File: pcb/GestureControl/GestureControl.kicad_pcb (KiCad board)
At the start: 4 copper layers, 95.3 x 87.6 mm, 102 parts, among them J1 Conn_01x04_I2I-LCD, J10 EXTERN I2C, J11 Conn_01x01, J12 Conn_01x01, J13 Conn_01x01, J14 Conn_01x01, J15 Conn_01x01, J16 Conn_01x01, J17 Conn_01x01, J18 Conn_01x01, J19 Conn_01x01, J2 BATT, J3 Conn_01x08, J4 Conn_01x06, J5 Conn_01x10, J6 Conn_01x08, J7 FTDI, J8 Serial Wire, J9 UART, SW1 SW1, SW2 SW2, SW3 BOOT, SW4 RST, U1 LD1117-3.3, U2 LD1117-5.0, U3 VL53L3CXV0DH_CENTER, U4 VL53L3CXV0DH_RIGHT, U5 VL53L3CXV0DH_LEFT, U6 STM32L151RETx, U7 STM32F401RETx, Y1 8MHz, Y2 32kHz

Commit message: eind tekenen PCB
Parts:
- C23, C28, C29, C30, C31, D7, R10, R11: moved to B.Cu
- J10: footprint Connector_PinHeader_2.54mm:PinHeader_1x04_P2.54mm_Horizontal -> Connector_PinHeader_2.54mm:PinHeader_1x04_P2.54mm_Vertical
- J7: footprint Connector_PinHeader_2.54mm:PinHeader_1x06_P2.54mm_Horizontal -> Connector_PinHeader_2.54mm:PinHeader_1x06_P2.54mm_Vertical
- J8: footprint Connector_PinHeader_2.54mm:PinHeader_1x05_P2.54mm_Horizontal -> Connector_PinHeader_2.54mm:PinHeader_1x05_P2.54mm_Vertical
- R1, R2, R3, R4, R5, R6, R7: moved to F.Cu
- moved J7 64.7 mm to (157.0, 63.8), turned to 180 degrees
- moved J8 46.2 mm to (153.2, 61.2), turned to 180 degrees
- moved D7 44.0 mm to (128.8, 101.1), turned to 180 degrees
- moved J19 37.2 mm to (164.3, 47.8), turned to 180 degrees
- moved C4 36.0 mm to (129.0, 89.9), turned to 0 degrees
- moved C3 35.2 mm to (139.4, 89.9), turned to 0 degrees
- moved J18 34.2 mm to (164.3, 50.3), turned to 180 degrees
- moved SW2 33.6 mm to (162.8, 78.2), turned to 180 degrees
- moved D5 31.5 mm to (156.7, 95.2), turned to 90 degrees
- moved C6 31.2 mm to (129.0, 97.3), turned to 0 degrees
- moved R5 30.5 mm to (156.7, 91.2), turned to 90 degrees
- moved R9 30.1 mm to (159.8, 75.9)
- moved C2 30.0 mm to (159.6, 78.0), turned to 180 degrees
- moved J17 29.9 mm to (164.3, 57.9)
- moved J16 28.9 mm to (164.3, 60.5), turned to 180 degrees
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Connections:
- U6 pad 27: (no net) -> SW_1
- U6 pad 28: (no net) -> SW_2
- U7 pad 27: (no net) -> SW_1
- U7 pad 28: (no net) -> SW_2
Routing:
- net GND: track 89.6 -> 206.3 mm, vias 45 -> 29
- net +3V3: track 399.3 -> 506.0 mm, vias 37 -> 21
- net /STM32L151RET6TR/SWDAT: track 80.6 -> 20.3 mm, vias 3 -> 1
- net LED_5: track 94.8 -> 37.5 mm, vias 3 -> 1
- net LED_4: track 95.3 -> 39.3 mm, vias 3 -> 1
- net /STM32L151RET6TR/SW0: track 62.4 -> 23.6 mm, vias 1 -> 2
- net /STM32L151RET6TR/FTDI_TXD: track 53.1 -> 15.6 mm, vias 3 -> 0
- net /STM32L151RET6TR/SWCLK: track 57.5 -> 22.9 mm, vias 1 -> 0
- net /STM32L151RET6TR/FTDI_CTS: track 55.5 -> 22.0 mm, vias 0 -> 1
- net /STM32L151RET6TR/FTDI_RXD: track 50.3 -> 16.9 mm, vias 3 -> 0
- net LED_3: track 73.1 -> 40.9 mm, vias 3 -> 1
- net VCC: track 26.7 -> 55.5 mm, vias 4 -> 6
- net /STM32L151RET6TR/OS32_IN: track 37.0 -> 9.26 mm
- net /STM32L151RET6TR/OS32_OUT: track 35.4 -> 9.99 mm
- net GPIOI_2: track 113.2 -> 90.9 mm
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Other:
- net class PWR added: clearance 0.4, trace_width 0.25, via_dia 0.8, via_drill 0.4
- board text removed: "- +"
- board text removed: "BOOT"
- board text removed: "FTDI"
- board text removed: "I2C LCD"
- board text removed: "RST"
- board text removed: "Serial Wire"
- board text removed: "UART"

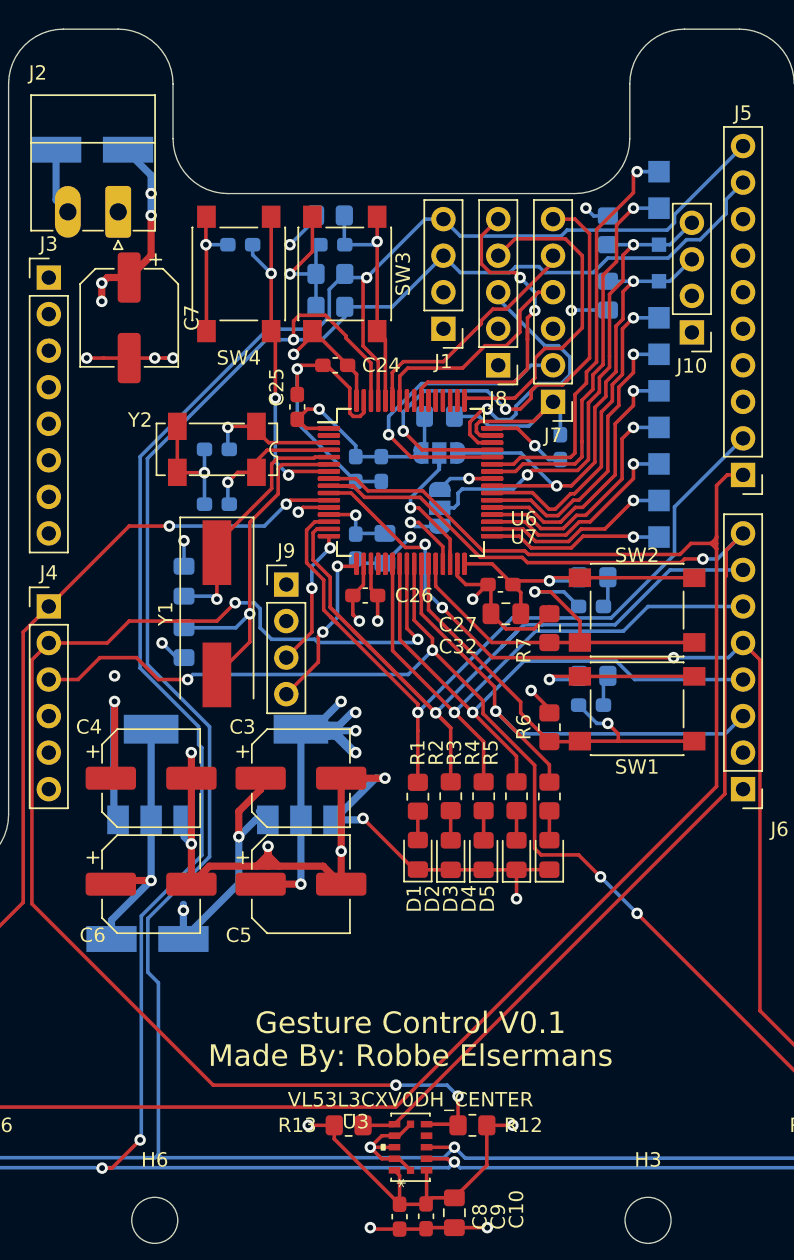
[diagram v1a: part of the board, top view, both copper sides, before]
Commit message: add text pcb
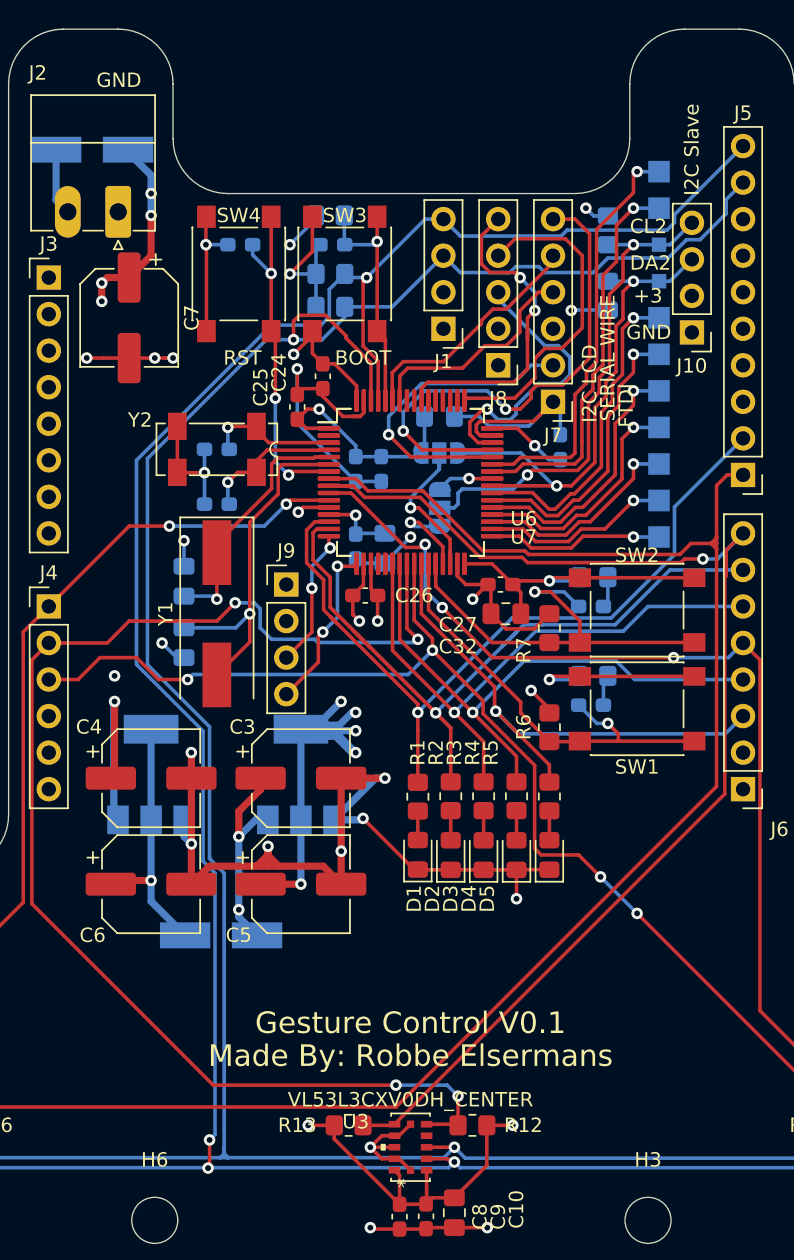
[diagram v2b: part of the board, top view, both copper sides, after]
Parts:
- moved D7 5.13 mm to (133.9, 100.8)
- moved C24 1.15 mm to (141.0, 62.0), turned to 270 degrees
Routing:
- net SCL1: track 195.7 -> 193.2 mm
- net GND: track 206.3 -> 205.5 mm
- net +3V3: track 506.0 -> 506.8 mm
- net +5V: track 109.6 -> 108.8 mm
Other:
- board text added: "+3"
- board text added: "+3.3"
- board text added: "+5"
- board text added: "-"
- board text added: "BOOT"
- board text added: "CL1"
- board text added: "CL2"
- board text added: "CLK"
- board text added: "CTS"
- board text added: "D1"
- board text added: "D2"
- board text added: "D3"
- board text added: "D4"
- board text added: "D5"
- board text added: "DA1"
- board text added: "DA2"
- board text added: "DAT"
- board text added: "F401RETx (U7): JP3 -> 1-2, JP2 -> 2-3"
- board text added: "FTDI"
- board text added: "GND"
- board text added: "GP0"
- board text added: "GP1"
- board text added: "GP2"
- board text added: "I2C LCD"
- board text added: "I2C Slave"
- board text added: "L151RETx (U6): JP3 -> 2-3, JP2 -> 1-2"
- board text added: "PA10 PA9 SCL2 SDA2 PC8 PC7 PC6 PB15 PB14 PB13 PB12"
- board text added: "RST"
- board text added: "RTS"
- board text added: "RX"
- board text added: "SERIAL WIRE"
- board text added: "SW0"
- board text added: "TX"
- board text added: "XS0"
- board text added: "XS1"
- board text added: "XS2"

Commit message: add feedback Philip
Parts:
- added C34: 4.7µ, Capacitor_SMD:C_0805_2012Metric_Pad1.18x1.45mm_HandSolder, F.Cu at (142.0, 102.9)
- added C35: 100n, Capacitor_SMD:C_0603_1608Metric_Pad1.08x0.95mm_HandSolder, B.Cu at (146.8, 111.4)
- added C36: 100n, Capacitor_SMD:C_0603_1608Metric_Pad1.08x0.95mm_HandSolder, B.Cu at (146.8, 128.4)
- added C37: 4.7µ, Capacitor_SMD:C_0805_2012Metric_Pad1.18x1.45mm_HandSolder, B.Cu at (148.8, 111.2)
- added C38: 4.7µ, Capacitor_SMD:C_0805_2012Metric_Pad1.18x1.45mm_HandSolder, B.Cu at (148.8, 128.2)
- added C39: 100n, Capacitor_SMD:C_0603_1608Metric_Pad1.08x0.95mm_HandSolder, B.Cu at (178.1, 128.5)
- added C40: 100n, Capacitor_SMD:C_0603_1608Metric_Pad1.08x0.95mm_HandSolder, B.Cu at (176.3, 111.4)
- added C41: 4.7µ, Capacitor_SMD:C_0805_2012Metric_Pad1.18x1.45mm_HandSolder, B.Cu at (180.1, 128.2)
- added C42: 4.7µ, Capacitor_SMD:C_0805_2012Metric_Pad1.18x1.45mm_HandSolder, B.Cu at (180.1, 111.2)
- added C43: 100n, Capacitor_SMD:C_0603_1608Metric_Pad1.08x0.95mm_HandSolder, B.Cu at (115.3, 128.5)
- added C44: 100n, Capacitor_SMD:C_0603_1608Metric_Pad1.08x0.95mm_HandSolder, B.Cu at (115.3, 111.4)
- added C45: 4.7µ, Capacitor_SMD:C_0805_2012Metric_Pad1.18x1.45mm_HandSolder, B.Cu at (119.1, 128.3)
- added C46: 4.7µ, Capacitor_SMD:C_0805_2012Metric_Pad1.18x1.45mm_HandSolder, B.Cu at (119.1, 111.2)
- added C47: 100n, Capacitor_SMD:C_0603_1608Metric_Pad1.08x0.95mm_HandSolder, B.Cu at (145.0, 111.4)
- added C48: 100n, Capacitor_SMD:C_0603_1608Metric_Pad1.08x0.95mm_HandSolder, B.Cu at (145.0, 128.4)
- added C49: 100n, Capacitor_SMD:C_0603_1608Metric_Pad1.08x0.95mm_HandSolder, B.Cu at (178.1, 111.4)
- added C50: 100n, Capacitor_SMD:C_0603_1608Metric_Pad1.08x0.95mm_HandSolder, B.Cu at (176.3, 128.5)
- added C51: 100n, Capacitor_SMD:C_0603_1608Metric_Pad1.08x0.95mm_HandSolder, B.Cu at (117.1, 111.4)
- added C52: 100n, Capacitor_SMD:C_0603_1608Metric_Pad1.08x0.95mm_HandSolder, B.Cu at (117.1, 128.6)
- added U10: VL53L3CXV0DH_RIGHT, VL53L3CX:VL53L3CXV0DH&slash_1, F.Cu at (177.5, 107.1)
- added U11: VL53L3CXV0DH_LEFT, VL53L3CX:VL53L3CXV0DH&slash_1, F.Cu at (116.6, 107.2)
- added U12: VL53L3CXV0DH_CENTER, VL53L3CX:VL53L3CXV0DH&slash_1, F.Cu at (146.5, 124.2)
- added U13: VL53L3CXV0DH_CENTER, VL53L3CX:VL53L3CXV0DH&slash_1, F.Cu at (146.5, 107.2)
- added U8: VL53L3CXV0DH_RIGHT, VL53L3CX:VL53L3CXV0DH&slash_1, F.Cu at (177.5, 124.2)
- added U9: VL53L3CXV0DH_LEFT, VL53L3CX:VL53L3CXV0DH&slash_1, F.Cu at (116.6, 124.2)
- C10, C11, C12, C13, C14, C15, C16, C8, C9, R12, R13, R14, R15, R16, R17: moved to B.Cu
- C17, C18, C19, C22: moved to F.Cu
- J8: value Serial Wire -> Conn_01x06; footprint Connector_PinHeader_2.54mm:PinHeader_1x05_P2.54mm_Vertical -> Connector_PinHeader_2.54mm:PinHeader_1x06_P2.54mm_Vertical
- moved R17 11.0 mm to (116.8, 115.3), turned to 90 degrees
- moved H5 7.41 mm to (189.0, 128.0)
- moved C12 7.37 mm to (176.3, 120.1)
- moved H2 7.37 mm to (103.9, 128.0)
- moved H3 7.37 mm to (163.6, 128.0)
- moved H6 7.37 mm to (129.3, 128.0)
- moved R14 7.01 mm to (180.1, 115.6), turned to 90 degrees
- moved U5 6.35 mm to (116.6, 115.6)
- moved C19 5.90 mm to (128.0, 69.0), turned to 270 degrees
- moved C15 5.88 mm to (115.3, 119.8)
- moved C14 5.87 mm to (117.1, 119.8)
- moved C16 5.86 mm to (119.1, 119.6)
- moved C22 5.83 mm to (128.0, 65.4), turned to 90 degrees
- moved U4 5.08 mm to (177.5, 115.7)
- moved R16 4.76 mm to (119.1, 115.3), turned to 90 degrees
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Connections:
- J8 pad 1: GND -> +3V3
- J8 pad 2: +3V3 -> /STM32L151RET6TR/SWCLK
- J8 pad 3: /STM32L151RET6TR/SWDAT -> GND
- J8 pad 4: /STM32L151RET6TR/SWCLK -> /STM32L151RET6TR/SWDAT
- J8 pad 5: /STM32L151RET6TR/SW0 -> /STM32L151RET6TR/RST
- U3 pad 8: (no net) -> Net-(U12-Pad8)
- U4 pad 8: (no net) -> Net-(U10-Pad8)
- U5 pad 8: (no net) -> Net-(U11-Pad8)
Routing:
- net +3V3: track 506.8 -> 786.6 mm, vias 21 -> 26
- net SCL1: track 193.2 -> 410.9 mm, vias 6 -> 13
- net SDA1: track 194.0 -> 385.5 mm, vias 4 -> 10
- net GND: track 205.5 -> 343.5 mm, vias 29 -> 40
- net GPIOI_1: track 92.4 -> 121.2 mm, vias 4 -> 5
- net XSHUT_1: track 86.3 -> 112.0 mm, vias 1 -> 2
- net GPIOI_2: track 90.9 -> 113.3 mm, vias 6 -> 5
- net /STM32L151RET6TR/RST: track 23.9 -> 42.2 mm, vias 3 -> 4
- net /STM32L151RET6TR/SWCLK: track 22.9 -> 5.96 mm
- net XSHUT_0: track 124.9 -> 141.5 mm, vias 0 -> 1
- net XSHUT_2: track 75.5 -> 91.8 mm, vias 3 -> 4
- net GPIOI_0: track 68.0 -> 84.0 mm, vias 4 -> 5
- net LED_2: track 62.9 -> 55.6 mm
- net /STM32L151RET6TR/SW0: track 23.6 -> 17.4 mm
- net /STM32L151RET6TR/OS32_IN: track 9.26 -> 14.7 mm, vias 1 -> 0
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- added copper zone on PWR, net +3V3
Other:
- board size 95.3 x 87.6 mm -> 95.3 x 95.3 mm

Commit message: add PCBV0.11
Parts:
- removed C11, C12, C20, C21: 100n, Capacitor_SMD:C_0603_1608Metric_Pad1.08x0.95mm_HandSolder
- removed J13, J14, J15, J16: Conn_01x01, TestPoint:TestPoint_Pad_1.5x1.5mm
- removed SW3: BOOT, Button_Switch_SMD:SW_Push_1P1T_NO_6x6mm_H9.5mm
- removed SW4: RST, Button_Switch_SMD:SW_Push_1P1T_NO_6x6mm_H9.5mm
- added C53: 4.7µ, Capacitor_SMD:C_0805_2012Metric_Pad1.18x1.45mm_HandSolder, B.Cu at (179.8, 111.2)
- added C54: 4.7µ, Capacitor_SMD:C_0805_2012Metric_Pad1.18x1.45mm_HandSolder, B.Cu at (179.8, 119.6)
- added C55: 4.7µ, Capacitor_SMD:C_0805_2012Metric_Pad1.18x1.45mm_HandSolder, B.Cu at (179.8, 128.2)
- added D8: B230A, Diode_SMD:D_SMA_Handsoldering, B.Cu at (128.2, 97.0)
- added JP1: SolderJumper_2_Open, Jumper:SolderJumper-2_P1.3mm_Open_Pad1.0x1.5mm, F.Cu at (127.8, 90.7)
- added JP10: SolderJumper_2_Open, Jumper:SolderJumper-2_P1.3mm_Open_Pad1.0x1.5mm, B.Cu at (168.0, 109.3)
- added JP11: SolderJumper_2_Open, Jumper:SolderJumper-2_P1.3mm_Open_Pad1.0x1.5mm, B.Cu at (159.4, 104.0)
- added JP12: SolderJumper_2_Open, Jumper:SolderJumper-2_P1.3mm_Open_Pad1.0x1.5mm, B.Cu at (159.4, 106.7)
- added JP14: SolderJumper_2_Open, Jumper:SolderJumper-2_P1.3mm_Open_Pad1.0x1.5mm, B.Cu at (159.4, 109.3)
- added JP15: SolderJumper_2_Open, Jumper:SolderJumper-2_P1.3mm_Open_Pad1.0x1.5mm, B.Cu at (142.7, 111.4)
- added JP16: SolderJumper_2_Open, Jumper:SolderJumper-2_P1.3mm_Open_Pad1.0x1.5mm, B.Cu at (142.7, 119.8)
- added JP17: SolderJumper_2_Open, Jumper:SolderJumper-2_P1.3mm_Open_Pad1.0x1.5mm, B.Cu at (142.7, 128.4)
- added JP18: SolderJumper_2_Open, Jumper:SolderJumper-2_P1.3mm_Open_Pad1.0x1.5mm, B.Cu at (151.8, 108.0)
- added JP19: SolderJumper_2_Open, Jumper:SolderJumper-2_P1.3mm_Open_Pad1.0x1.5mm, B.Cu at (151.8, 105.2)
- added JP20: SolderJumper_2_Open, Jumper:SolderJumper-2_P1.3mm_Open_Pad1.0x1.5mm, B.Cu at (152.0, 116.3)
- added JP21: SolderJumper_2_Open, Jumper:SolderJumper-2_P1.3mm_Open_Pad1.0x1.5mm, B.Cu at (152.0, 113.5)
- added JP22: SolderJumper_2_Open, Jumper:SolderJumper-2_P1.3mm_Open_Pad1.0x1.5mm, B.Cu at (151.9, 125.0)
- added JP23: SolderJumper_2_Open, Jumper:SolderJumper-2_P1.3mm_Open_Pad1.0x1.5mm, B.Cu at (151.9, 122.2)
- added JP27: SolderJumper_2_Open, Jumper:SolderJumper-2_P1.3mm_Open_Pad1.0x1.5mm, B.Cu at (173.7, 111.4)
- added JP28: SolderJumper_2_Open, Jumper:SolderJumper-2_P1.3mm_Open_Pad1.0x1.5mm, B.Cu at (173.7, 119.8)
- added JP29: SolderJumper_2_Open, Jumper:SolderJumper-2_P1.3mm_Open_Pad1.0x1.5mm, B.Cu at (173.7, 128.4)
- added JP30: SolderJumper_2_Open, Jumper:SolderJumper-2_P1.3mm_Open_Pad1.0x1.5mm, B.Cu at (182.7, 108.0)
- added JP31: SolderJumper_2_Open, Jumper:SolderJumper-2_P1.3mm_Open_Pad1.0x1.5mm, B.Cu at (182.7, 105.2)
- added JP32: SolderJumper_2_Open, Jumper:SolderJumper-2_P1.3mm_Open_Pad1.0x1.5mm, B.Cu at (182.7, 116.5)
- added JP33: SolderJumper_2_Open, Jumper:SolderJumper-2_P1.3mm_Open_Pad1.0x1.5mm, B.Cu at (182.7, 113.7)
- added JP34: SolderJumper_2_Open, Jumper:SolderJumper-2_P1.3mm_Open_Pad1.0x1.5mm, B.Cu at (182.8, 124.8)
- added JP35: SolderJumper_2_Open, Jumper:SolderJumper-2_P1.3mm_Open_Pad1.0x1.5mm, B.Cu at (182.7, 122.0)
- added JP36: SolderJumper_2_Open, Jumper:SolderJumper-2_P1.3mm_Open_Pad1.0x1.5mm, B.Cu at (113.0, 111.4)
- added JP37: SolderJumper_2_Open, Jumper:SolderJumper-2_P1.3mm_Open_Pad1.0x1.5mm, B.Cu at (113.0, 119.8)
- added JP38: SolderJumper_2_Open, Jumper:SolderJumper-2_P1.3mm_Open_Pad1.0x1.5mm, B.Cu at (113.0, 128.5)
- added JP39: SolderJumper_2_Open, Jumper:SolderJumper-2_P1.3mm_Open_Pad1.0x1.5mm, B.Cu at (122.3, 108.0)
- added JP4: SolderJumper_2_Open, Jumper:SolderJumper-2_P1.3mm_Open_Pad1.0x1.5mm, B.Cu at (139.4, 96.9)
- added JP40: SolderJumper_2_Open, Jumper:SolderJumper-2_P1.3mm_Open_Pad1.0x1.5mm, B.Cu at (122.3, 105.2)
- added JP41: SolderJumper_2_Open, Jumper:SolderJumper-2_P1.3mm_Open_Pad1.0x1.5mm, B.Cu at (122.3, 116.3)
- added JP42: SolderJumper_2_Open, Jumper:SolderJumper-2_P1.3mm_Open_Pad1.0x1.5mm, B.Cu at (122.2, 113.5)
- added JP43: SolderJumper_2_Open, Jumper:SolderJumper-2_P1.3mm_Open_Pad1.0x1.5mm, B.Cu at (122.2, 125.0)
- added JP44: SolderJumper_2_Open, Jumper:SolderJumper-2_P1.3mm_Open_Pad1.0x1.5mm, B.Cu at (122.2, 122.2)
- added JP5: SolderJumper_2_Open, Jumper:SolderJumper-2_P1.3mm_Open_Pad1.0x1.5mm, B.Cu at (108.1, 111.6)
- added JP6: SolderJumper_2_Open, Jumper:SolderJumper-2_P1.3mm_Open_Pad1.0x1.5mm, B.Cu at (108.1, 114.3)
- added JP7: SolderJumper_2_Open, Jumper:SolderJumper-2_P1.3mm_Open_Pad1.0x1.5mm, B.Cu at (108.1, 117.0)
- added JP8: SolderJumper_2_Open, Jumper:SolderJumper-2_P1.3mm_Open_Pad1.0x1.5mm, B.Cu at (168.0, 104.0)
- added JP9: SolderJumper_2_Open, Jumper:SolderJumper-2_P1.3mm_Open_Pad1.0x1.5mm, B.Cu at (168.0, 106.7)
- added L1: 10µH, Inductor_SMD:L_Taiyo-Yuden_NR-50xx_HandSoldering, F.Cu at (134.6, 96.5)
- added L2: 10µH, Inductor_SMD:L_Taiyo-Yuden_NR-50xx_HandSoldering, B.Cu at (130.3, 91.2)
- added R18: 220, Resistor_SMD:R_0805_2012Metric_Pad1.20x1.40mm_HandSolder, F.Cu at (139.7, 87.4)
- added R19: 820, Resistor_SMD:R_0805_2012Metric_Pad1.20x1.40mm_HandSolder, B.Cu at (141.5, 94.0)
- added R23: 100, Resistor_SMD:R_0805_2012Metric_Pad1.20x1.40mm_HandSolder, F.Cu at (139.5, 91.2)
- added R24: 100, Resistor_SMD:R_0805_2012Metric_Pad1.20x1.40mm_HandSolder, B.Cu at (134.4, 92.9)
- added R25: 18k, Resistor_SMD:R_0805_2012Metric_Pad1.20x1.40mm_HandSolder, F.Cu at (135.6, 87.4)
- added R26: 10k, Resistor_SMD:R_0805_2012Metric_Pad1.20x1.40mm_HandSolder, B.Cu at (141.5, 91.7)
- added R27: 56k, Resistor_SMD:R_0805_2012Metric_Pad1.20x1.40mm_HandSolder, F.Cu at (131.6, 87.4)
- added R28: 56k, Resistor_SMD:R_0805_2012Metric_Pad1.20x1.40mm_HandSolder, B.Cu at (141.5, 89.4)
- added R29: 10k, Resistor_SMD:R_0805_2012Metric_Pad1.20x1.40mm_HandSolder, B.Cu at (146.6, 115.3)
- added R30: 10k, Resistor_SMD:R_0805_2012Metric_Pad1.20x1.40mm_HandSolder, B.Cu at (148.8, 124.2)
- added R31: 10k, Resistor_SMD:R_0805_2012Metric_Pad1.20x1.40mm_HandSolder, B.Cu at (179.8, 115.6)
- added R32: 10k, Resistor_SMD:R_0805_2012Metric_Pad1.20x1.40mm_HandSolder, B.Cu at (179.8, 107.2)
- added R33: 10k, Resistor_SMD:R_0805_2012Metric_Pad1.20x1.40mm_HandSolder, B.Cu at (177.5, 115.6)
- added R34: 10k, Resistor_SMD:R_0805_2012Metric_Pad1.20x1.40mm_HandSolder, B.Cu at (179.8, 124.2)
- added R35: 10k, Resistor_SMD:R_0805_2012Metric_Pad1.20x1.40mm_HandSolder, B.Cu at (116.8, 115.3)
- added R36: 10k, Resistor_SMD:R_0805_2012Metric_Pad1.20x1.40mm_HandSolder, B.Cu at (119.1, 124.2)
- C13: value 4.7µ -> 10µ; footprint Capacitor_SMD:C_0805_2012Metric_Pad1.18x1.45mm_HandSolder -> Capacitor_SMD:C_1206_3216Metric_Pad1.33x1.80mm_HandSolder; moved to F.Cu
- C3: value 10µ -> 10µF; footprint Capacitor_SMD:CP_Elec_6.3x5.4 -> Capacitor_SMD:C_1206_3216Metric_Pad1.33x1.80mm_HandSolder
- C34: value 4.7µ -> 10µ; footprint Capacitor_SMD:C_0805_2012Metric_Pad1.18x1.45mm_HandSolder -> Capacitor_SMD:C_1206_3216Metric_Pad1.33x1.80mm_HandSolder; moved to B.Cu
- C4: value 10µ -> 10µF; footprint Capacitor_SMD:CP_Elec_6.3x5.4 -> Capacitor_SMD:C_1206_3216Metric_Pad1.33x1.80mm_HandSolder; moved to B.Cu
- C41, C42: value 4.7µ -> 100n; footprint Capacitor_SMD:C_0805_2012Metric_Pad1.18x1.45mm_HandSolder -> Capacitor_SMD:C_0603_1608Metric_Pad1.08x0.95mm_HandSolder
- C5: value 100µ -> 100nF; footprint Capacitor_SMD:CP_Elec_6.3x5.4 -> Capacitor_SMD:C_0603_1608Metric_Pad1.08x0.95mm_HandSolder
- C6: value 100µ -> 100nF; footprint Capacitor_SMD:CP_Elec_6.3x5.4 -> Capacitor_SMD:C_0603_1608Metric_Pad1.08x0.95mm_HandSolder; moved to B.Cu
- D7: value 1N4002 -> B230A; moved to F.Cu
- J11, J12: value Conn_01x01 -> Conn_01x02; footprint TestPoint:TestPoint_Pad_1.5x1.5mm -> Connector_PinHeader_2.54mm:PinHeader_1x02_P2.54mm_Vertical; moved to F.Cu
- R10, R11: moved to F.Cu
- R14: value 10k -> 100k; moved to F.Cu
- R15: value 10k -> 100k
- U1: value LD1117-3.3 -> AP5100_3.3; footprint Package_TO_SOT_SMD:SOT-223-3_TabPin2 -> Package_TO_SOT_SMD:TSOT-23-6_HandSoldering; moved to F.Cu
- U2: value LD1117-5.0 -> AP5100_3.3; footprint Package_TO_SOT_SMD:SOT-223-3_TabPin2 -> Package_TO_SOT_SMD:TSOT-23-6_HandSoldering
- moved C13 56.5 mm to (127.5, 99.3), turned to 90 degrees
- moved R14 56.3 mm to (127.8, 94.7), turned to 270 degrees
- moved R15 44.8 mm to (136.9, 97.3), turned to 270 degrees
- moved J11 33.4 mm to (141.7, 48.5), turned to 0 degrees
- moved J12 29.0 mm to (145.5, 48.5), turned to 0 degrees
- moved C34 20.1 mm to (125.5, 91.4), turned to 270 degrees
- moved C39 17.3 mm to (176.0, 111.4)
- moved C44 17.2 mm to (117.1, 128.5)
- moved C43 17.1 mm to (115.3, 111.4)
- moved C45 17.1 mm to (119.1, 111.2)
- moved C46 17.1 mm to (119.1, 128.3)
- moved C22 16.2 mm to (142.5, 58.2), turned to 270 degrees
- moved C19 12.7 mm to (134.9, 58.3)
- moved Y2 11.1 mm to (138.7, 57.1), turned to 90 degrees
- moved R20 11.0 mm to (144.0, 61.5)
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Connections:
- C10 pad 1: +3V3 -> /VL53L3CX center/PWR1
- C14 pad 1: +3V3 -> /VL53L3CX left/PWR1
- C15 pad 1: +3V3 -> /VL53L3CX left/PWR1
- C16 pad 1: +3V3 -> /VL53L3CX left/PWR1
- C3 pad 1: +5V -> VCC
- C34 pad 1: +3V3 -> +5V
- C35 pad 1: +3V3 -> /VL53L3CX center/PWR0
- C36 pad 1: +3V3 -> /VL53L3CX center/PWR2
- C37 pad 1: +3V3 -> /VL53L3CX center/PWR0
- C38 pad 1: +3V3 -> /VL53L3CX center/PWR2
- C39 pad 1: +3V3 -> /VL53L3CX right/PWR0
- C40 pad 1: +3V3 -> /VL53L3CX right/PWR1
- C41 pad 1: +3V3 -> /VL53L3CX right/PWR2
- C42 pad 1: +3V3 -> /VL53L3CX right/PWR0
- C43 pad 1: +3V3 -> /VL53L3CX left/PWR0
- C44 pad 1: +3V3 -> /VL53L3CX left/PWR2
- C45 pad 1: +3V3 -> /VL53L3CX left/PWR0
- C46 pad 1: +3V3 -> /VL53L3CX left/PWR2
- C47 pad 1: +3V3 -> /VL53L3CX center/PWR0
- C48 pad 1: +3V3 -> /VL53L3CX center/PWR2
- C49 pad 1: +3V3 -> /VL53L3CX right/PWR1
- C5 pad 1: +3V3 -> Net-(C5-Pad1)
- C5 pad 2: GND -> Net-(C5-Pad2)
- C50 pad 1: +3V3 -> /VL53L3CX right/PWR2
- C51 pad 1: +3V3 -> /VL53L3CX left/PWR0
- C52 pad 1: +3V3 -> /VL53L3CX left/PWR2
- C6 pad 2: GND -> Net-(C6-Pad2)
- C8 pad 1: +3V3 -> /VL53L3CX center/PWR1
- C9 pad 1: +3V3 -> /VL53L3CX center/PWR1
- D7 pad 1: +5V -> /OUT3.3
- D7 pad 2: Net-(C6-Pad1) -> GND
- J11 pad 1: /STM32L151RET6TR/PB12 -> GND
- J12 pad 1: /STM32L151RET6TR/PB13 -> +3V3
- J4 pad 4: (no net) -> _XSHUT_0
- J4 pad 5: (no net) -> _XSHUT_3
- J4 pad 6: (no net) -> _XSHUT_6
- J5 pad 1: XSHUT_0 -> _XSHUT_1
- J5 pad 3: (no net) -> _XSHUT_8
- J5 pad 4: (no net) -> _XSHUT_5
- J5 pad 5: (no net) -> _XSHUT_2
- J6 pad 5: XSHUT_2 -> _XSHUT_7
- J6 pad 8: XSHUT_1 -> _XSHUT_4
- R13 pad 1: +3V3 -> /VL53L3CX center/PWR0
- R14 pad 1: +3V3 -> VCC
- R14 pad 2: GPIOI_2 -> Net-(JP1-Pad1)
- R15 pad 1: +3V3 -> VCC
- R15 pad 2: XSHUT_2 -> Net-(JP4-Pad1)
- R17 pad 1: +3V3 -> /VL53L3CX left/PWR0
- U1 pad 1: GND -> Net-(C5-Pad2)
- U1 pad 2: +3V3 -> GND
- U1 pad 3: +5V -> Net-(R25-Pad1)
- U10 pad 1: +3V3 -> /VL53L3CX right/PWR0
- U10 pad 10: SCL1 -> Net-(JP30-Pad1)
- U10 pad 11: +3V3 -> /VL53L3CX right/PWR0
- U10 pad 8: Net-(U10-Pad8) -> (no net)
- U10 pad 9: SDA1 -> Net-(JP31-Pad1)
- U11 pad 1: +3V3 -> /VL53L3CX left/PWR0
- U11 pad 10: SCL1 -> Net-(JP39-Pad1)
- U11 pad 11: +3V3 -> /VL53L3CX left/PWR0
- U11 pad 8: Net-(U11-Pad8) -> (no net)
- U11 pad 9: SDA1 -> Net-(JP40-Pad1)
- U12 pad 1: +3V3 -> /VL53L3CX center/PWR2
- U12 pad 10: SCL1 -> Net-(JP22-Pad1)
- U12 pad 11: +3V3 -> /VL53L3CX center/PWR2
- U12 pad 5: XSHUT_1 -> XSHUT_7
- U12 pad 8: Net-(U12-Pad8) -> (no net)
- U12 pad 9: SDA1 -> Net-(JP23-Pad1)
- U13 pad 1: +3V3 -> /VL53L3CX center/PWR0
- U13 pad 10: SCL1 -> Net-(JP18-Pad1)
- U13 pad 11: +3V3 -> /VL53L3CX center/PWR0
- U13 pad 8: Net-(U12-Pad8) -> (no net)
- U13 pad 9: SDA1 -> Net-(JP19-Pad1)
- U2 pad 1: GND -> Net-(C6-Pad2)
- U2 pad 2: Net-(C6-Pad1) -> GND
- U2 pad 3: VCC -> Net-(R26-Pad1)
- U3 pad 1: +3V3 -> /VL53L3CX center/PWR1
- U3 pad 10: SCL1 -> Net-(JP20-Pad1)
- U3 pad 11: +3V3 -> /VL53L3CX center/PWR1
- U3 pad 5: XSHUT_1 -> XSHUT_4
- U3 pad 8: Net-(U12-Pad8) -> (no net)
- U3 pad 9: SDA1 -> Net-(JP21-Pad1)
- U4 pad 1: +3V3 -> /VL53L3CX right/PWR1
- U4 pad 10: SCL1 -> Net-(JP32-Pad1)
- U4 pad 11: +3V3 -> /VL53L3CX right/PWR1
- U4 pad 5: XSHUT_2 -> XSHUT_5
- U4 pad 8: Net-(U10-Pad8) -> (no net)
- U4 pad 9: SDA1 -> Net-(JP33-Pad1)
- U5 pad 1: +3V3 -> /VL53L3CX left/PWR1
- U5 pad 10: SCL1 -> Net-(JP41-Pad1)
- U5 pad 11: +3V3 -> /VL53L3CX left/PWR1
- U5 pad 5: XSHUT_0 -> XSHUT_3
- U5 pad 8: Net-(U11-Pad8) -> (no net)
- U5 pad 9: SDA1 -> Net-(JP42-Pad1)
- U6 pad 10: XSHUT_2 -> _XSHUT_6
- U6 pad 2: (no net) -> BUCK_5_EN
- U6 pad 33: /STM32L151RET6TR/PB12 -> _XSHUT_7
- U6 pad 34: /STM32L151RET6TR/PB13 -> _XSHUT_4
- U6 pad 35: /STM32L151RET6TR/PB14 -> _XSHUT_1
- U6 pad 36: /STM32L151RET6TR/PB15 -> _XSHUT_8
- U6 pad 37: /STM32L151RET6TR/PC6 -> _XSHUT_5
- U6 pad 38: /STM32L151RET6TR/PC7 -> _XSHUT_2
- U6 pad 8: XSHUT_0 -> _XSHUT_0
- U6 pad 9: XSHUT_1 -> _XSHUT_3
- U7 pad 10: XSHUT_2 -> _XSHUT_6
- U7 pad 2: (no net) -> BUCK_5_EN
- U7 pad 33: /STM32L151RET6TR/PB12 -> _XSHUT_7
- U7 pad 34: /STM32L151RET6TR/PB13 -> _XSHUT_4
- U7 pad 35: /STM32L151RET6TR/PB14 -> _XSHUT_1
- U7 pad 36: /STM32L151RET6TR/PB15 -> _XSHUT_8
- U7 pad 37: /STM32L151RET6TR/PC6 -> _XSHUT_5
- U7 pad 38: /STM32L151RET6TR/PC7 -> _XSHUT_2
- U7 pad 8: XSHUT_0 -> _XSHUT_0
- U7 pad 9: XSHUT_1 -> _XSHUT_3
- U8 pad 1: +3V3 -> /VL53L3CX right/PWR2
- U8 pad 10: SCL1 -> Net-(JP34-Pad1)
- U8 pad 11: +3V3 -> /VL53L3CX right/PWR2
- U8 pad 5: XSHUT_2 -> XSHUT_8
- U8 pad 8: Net-(U10-Pad8) -> (no net)
- U8 pad 9: SDA1 -> Net-(JP35-Pad1)
- U9 pad 1: +3V3 -> /VL53L3CX left/PWR2
- U9 pad 10: SCL1 -> Net-(JP43-Pad1)
- U9 pad 11: +3V3 -> /VL53L3CX left/PWR2
- U9 pad 5: XSHUT_0 -> XSHUT_6
- U9 pad 8: Net-(U11-Pad8) -> (no net)
- U9 pad 9: SDA1 -> Net-(JP44-Pad1)
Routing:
- net +3V3: track 786.6 -> 516.1 mm, vias 26 -> 33
- net SDA1: track 385.5 -> 248.2 mm, vias 10 -> 3
- net SCL1: track 410.9 -> 274.9 mm, vias 13 -> 16
- net XSHUT_0: track 141.5 -> 16.0 mm, vias 1 -> 2
- net XSHUT_1: track 112.0 -> 21.7 mm
- net GND: track 343.5 -> 257.3 mm, vias 40 -> 46
- net XSHUT_2: track 91.8 -> 13.5 mm, vias 4 -> 1
- net _XSHUT_5: track 0.00 -> 75.8 mm, vias 0 -> 1
- net _XSHUT_2: track 0.00 -> 75.1 mm, vias 0 -> 1
- net _XSHUT_8: track 0.00 -> 73.2 mm, vias 0 -> 1
- net _XSHUT_0: track 0.00 -> 65.3 mm, vias 0 -> 1
- net _XSHUT_3: track 0.00 -> 64.0 mm, vias 0 -> 1
- net _XSHUT_6: track 0.00 -> 63.9 mm, vias 0 -> 1
- net _XSHUT_1: track 0.00 -> 61.3 mm, vias 0 -> 1
- net _XSHUT_4: track 0.00 -> 57.5 mm, vias 0 -> 1
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- added copper zone on F.Cu, net +3V3
- added copper zone on F.Cu, net /OUT3.3
- added copper zone on B.Cu, net /OUT5.0
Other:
- net class PWR: clearance 0.4 -> 0.3
- board text added: "PA10 PA9 SCL2 SDA2 PC8"
- board text removed: "+3.3"
- board text removed: "PA10 PA9 SCL2 SDA2 PC8 PC7 PC6 PB15 PB14 PB13 PB12"

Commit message: update board design
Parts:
- added C11: 4.7µF, Capacitor_SMD:C_0805_2012Metric_Pad1.18x1.45mm_HandSolder, B.Cu at (141.7, 78.5)
- added C12: 4.7µF, Capacitor_SMD:C_0805_2012Metric_Pad1.18x1.45mm_HandSolder, B.Cu at (160.5, 100.8)
- moved R18 0.76 mm to (139.7, 86.6)
- moved JP14 0.38 mm to (159.4, 109.7)
- moved JP12 0.25 mm to (159.4, 106.9)
- moved JP11 0.13 mm to (159.4, 104.1)
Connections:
- J3 pad 1: (no net) -> Net-(J3-Pad1)
- J3 pad 2: (no net) -> Net-(J3-Pad2)
- J3 pad 3: (no net) -> Net-(J3-Pad3)
- J3 pad 8: (no net) -> Net-(J3-Pad8)
- J5 pad 6: (no net) -> Net-(J5-Pad6)
- J6 pad 1: (no net) -> Net-(J6-Pad1)
- J6 pad 2: (no net) -> Net-(J6-Pad2)
- U10 pad 8: (no net) -> Net-(U10-Pad8)
- U11 pad 8: (no net) -> Net-(U11-Pad8)
- U12 pad 8: (no net) -> Net-(U12-Pad8)
- U13 pad 8: (no net) -> Net-(U13-Pad8)
- U3 pad 8: (no net) -> Net-(U3-Pad8)
- U4 pad 8: (no net) -> Net-(U4-Pad8)
- U5 pad 8: (no net) -> Net-(U5-Pad8)
- U6 pad 20: (no net) -> Net-(U6-Pad20)
- U6 pad 21: (no net) -> Net-(U6-Pad21)
- U6 pad 50: (no net) -> Net-(U6-Pad50)
- U6 pad 51: (no net) -> Net-(U6-Pad51)
- U6 pad 52: (no net) -> Net-(U6-Pad52)
- U6 pad 53: (no net) -> Net-(U6-Pad53)
- U6 pad 54: (no net) -> Net-(U6-Pad54)
- U6 pad 56: (no net) -> Net-(U6-Pad56)
- U6 pad 57: (no net) -> Net-(U6-Pad57)
- U7 pad 20: (no net) -> Net-(U7-Pad20)
- U7 pad 21: (no net) -> Net-(U7-Pad21)
- U7 pad 50: (no net) -> Net-(U7-Pad50)
- U7 pad 51: (no net) -> Net-(U7-Pad51)
- U7 pad 52: (no net) -> Net-(U7-Pad52)
- U7 pad 53: (no net) -> Net-(U7-Pad53)
- U7 pad 54: (no net) -> Net-(U7-Pad54)
- U7 pad 56: (no net) -> Net-(U7-Pad56)
- U7 pad 57: (no net) -> Net-(U7-Pad57)
- U8 pad 8: (no net) -> Net-(U8-Pad8)
- U9 pad 8: (no net) -> Net-(U9-Pad8)
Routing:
- net GND: track 257.3 -> 303.0 mm, vias 46 -> 58
- net SCL1: track 274.9 -> 263.4 mm
- net Net-(JP21-Pad1): track 10.4 -> 17.3 mm
- net VCC: track 93.8 -> 99.5 mm
- net _XSHUT_1: track 61.3 -> 58.2 mm, vias 1 -> 2
- net _XSHUT_3: track 64.0 -> 66.7 mm
- net _XSHUT_0: track 65.3 -> 68.0 mm
- net _XSHUT_6: track 63.9 -> 66.5 mm
- net GPIOI_0: track 100.6 -> 98.2 mm
- net _XSHUT_2: track 75.1 -> 73.3 mm
- net _XSHUT_5: track 75.8 -> 74.1 mm
- net GPIOI_1: track 114.1 -> 115.7 mm
- net /STM32L151RET6TR/FTDI_RTS: track 35.6 -> 34.1 mm
- net SDA1: track 248.2 -> 249.7 mm
- net GPIOI_2: track 123.5 -> 124.9 mm
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- added copper zone on B.Cu, net GND
- added copper zone on F.Cu, net GND
